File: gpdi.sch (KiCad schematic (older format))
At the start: 20 parts, among them U1 LFE5U-85F-6BG381C, U11 PCA9306D

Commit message: schematics: some PN's for LCSC
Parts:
- GPDI1: LCSC (none) -> C427307
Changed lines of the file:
@@
 F 11 "609-4614-1-ND" H 8950 2950 50  0001 C CNN "Digikey"
 F 12 "A136174CT-ND" H 8950 2950 50  0001 C CNN "Digike_y2"
-F 13 "10029449-111RLF" H 8950 2950 50  0001 C CNN "Onlinecomponents"
-F 14 "0.364$" H 8950 2950 50  0001 C CNN "price100_Onlinecomponents"
-F 15 "FX001" H 8950 2950 50  0001 C CNN "Koncar"
-F 16 "T" H 8950 2950 50  0001 C CNN "Side"
+F 13 "C427307" H 8950 2950 50  0001 C CNN "LCSC"
+F 14 "10029449-111RLF" H 8950 2950 50  0001 C CNN "Onlinecomponents"
+F 15 "0.364$" H 8950 2950 50  0001 C CNN "price100_Onlinecomponents"
+F 16 "FX001" H 8950 2950 50  0001 C CNN "Koncar"
+F 17 "T" H 8950 2950 50  0001 C CNN "Side"
 	1    8950 2950
 	1    0    0    -1

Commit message: LCSC PN's
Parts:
- R24: LCSC (none) -> C73806
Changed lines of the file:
@@
 F 7 "71-CRCW0603100KFKEAC" V 6100 4700 50  0001 C CNN "Mouse_r2"
 F 8 "P100KHCT-ND" V 6100 4700 50  0001 C CNN "Digikey"
-F 9 "FR003" V 6100 4700 50  0001 C CNN "Koncar"
+F 9 "C73806" V 6100 4700 50  0001 C CNN "LCSC"
+F 10 "FR003" V 6100 4700 50  0001 C CNN "Koncar"
 	1    6100 4700
 	1    0    0    -1

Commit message: schematics: switch to serdes symbol
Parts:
- U1: symbol lfe5bg381:LFE5U-85F-6BG381C -> lfe5bg381:LFE5UM-85F-6BG381C
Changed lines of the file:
@@
 	6100 4450 6300 4450
 $Comp
-L lfe5bg381:LFE5U-85F-6BG381C U1
+L lfe5bg381:LFE5UM-85F-6BG381C U1
 U 2 1 5A07A906
 P 3600 2900

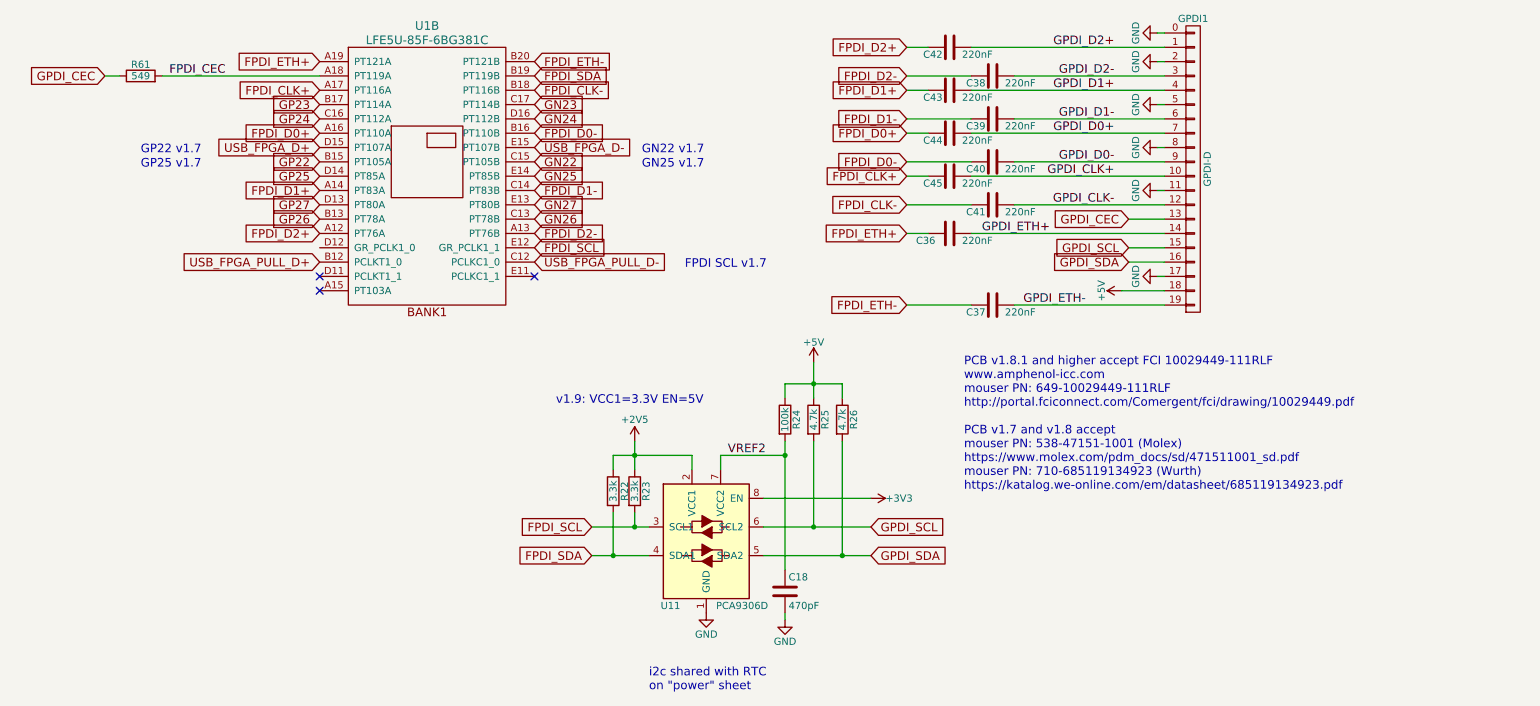
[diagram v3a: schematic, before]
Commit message: schematics: HPD resistor instead of capacitor
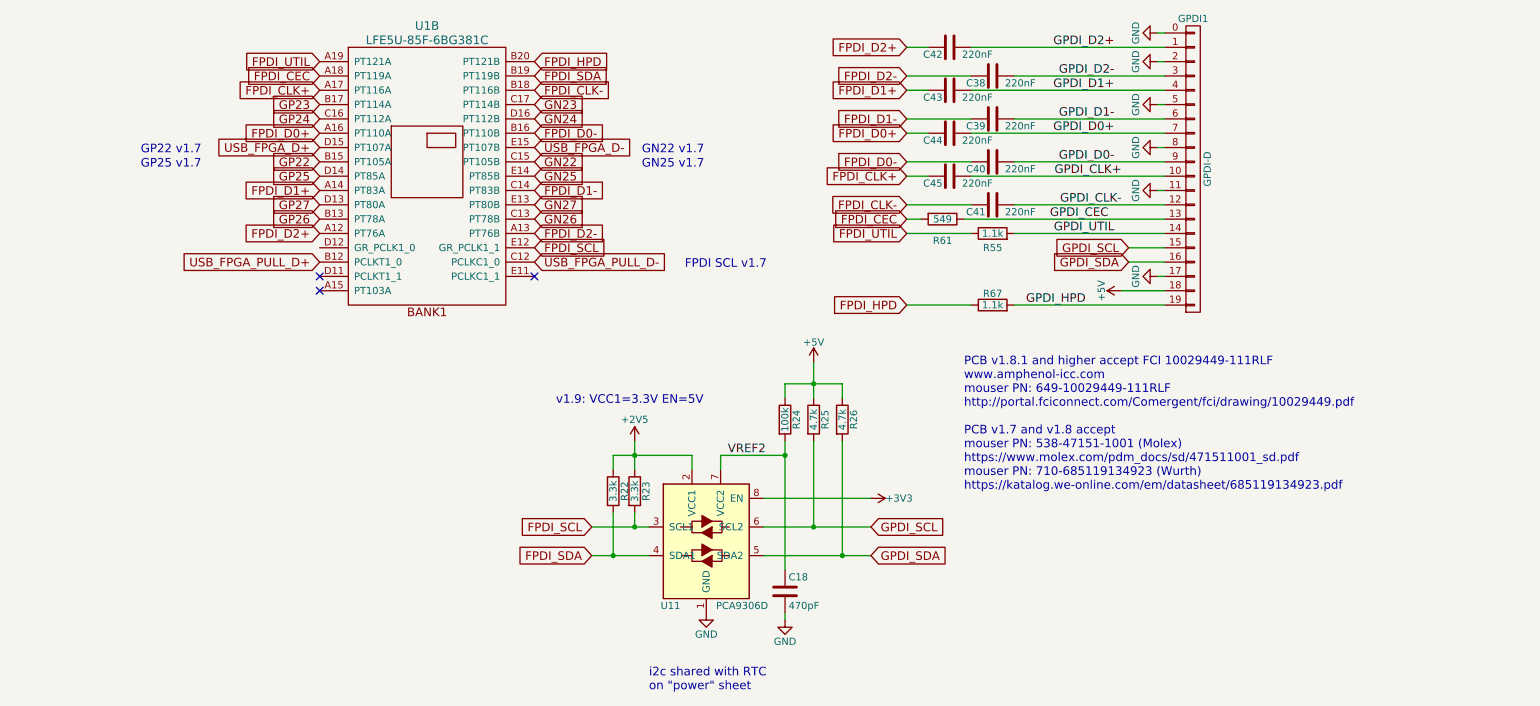
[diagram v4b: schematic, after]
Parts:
- removed C36, C37: 220nF, Capacitor_SMD:C_0603_1608Metric, symbol Device:C
- added R55, R67: 1.1k, Resistor_SMD:R_0603_1608Metric, symbol Device:R
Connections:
- net FPDI_ETH+ renamed FPDI_UTIL
- net FPDI_UTIL: now also R55.1
- net FPDI_ETH- renamed FPDI_HPD
- net FPDI_HPD: now also R67.1
- net GPDI_ETH+ renamed GPDI_UTIL
- net GPDI_UTIL: now also R55.2
- net GPDI_ETH- renamed GPDI_HPD
- net GPDI_HPD: now also R67.2
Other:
- moved on the sheet: R61
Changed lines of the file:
@@
 Title "ULX3S"
 Date ""
-Rev "1.0.2"
+Rev "1.0.3"
 Comp "EMARD"
 Comment1 "General Purpose Differential Interface"
@@
 $EndComp
 Text GLabel 6950 3900 0    60   Input ~ 0
-FPDI_ETH-
+FPDI_HPD
 Text GLabel 6950 3400 0    60   Input ~ 0
-FPDI_ETH+
+FPDI_UTIL
 Text GLabel 6950 2100 0    60   Input ~ 0
 FPDI_D2+
@@
 Text GLabel 6950 3200 0    60   Input ~ 0
 FPDI_CLK-
-Text GLabel 8500 3300 0    60   Input ~ 0
-GPDI_CEC
+Text GLabel 6950 3300 0    60   Input ~ 0
+FPDI_CEC
 Text GLabel 8500 3500 0    60   Input ~ 0
 GPDI_SCL
@@
 FPDI_CLK-
 Text GLabel 4350 2200 2    60   Input ~ 0
-FPDI_ETH-
+FPDI_HPD
 Text GLabel 2850 3100 0    60   Input ~ 0
 FPDI_D1+
@@
 FPDI_CLK+
 Text GLabel 2850 2200 0    60   Input ~ 0
-FPDI_ETH+
+FPDI_UTIL
 Text GLabel 4350 3500 2    60   Input ~ 0
 FPDI_SCL
 Text GLabel 4350 2300 2    60   Input ~ 0
 FPDI_SDA
-Text GLabel 1350 2300 0    60   Input ~ 0
-GPDI_CEC
+Text GLabel 2850 2300 0    60   Input ~ 0
+FPDI_CEC
 Text GLabel 4350 2900 2    60   Input ~ 0
 GN22
@@
 	8750 3200 7700 3200
 Wire Wire Line
-	8750 3300 8500 3300
-Wire Wire Line
-	8750 3400 7400 3400
+	8750 3400 7700 3400
 Wire Wire Line
 	8750 3500 8500 3500
@@
 L Device:R R61
 U 1 1 5A0777ED
-P 1600 2300
-F 0 "R61" V 1680 2300 50  0000 C CNN
-F 1 "549" V 1600 2300 50  0000 C CNN
-F 2 "Resistor_SMD:R_0603_1608Metric" V 1530 2300 50  0001 C CNN
-F 3 "" H 1600 2300 50  0000 C CNN
-	1    1600 2300
-	0    -1   -1   0
-$EndComp
-Wire Wire Line
-	1750 2300 2850 2300
-Wire Wire Line
-	1450 2300 1350 2300
-Text Label 1800 2300 0    60   ~ 0
-FPDI_CEC
+P 7200 3300
+F 0 "R61" V 7350 3300 50  0000 C CNN
+F 1 "549" V 7200 3300 50  0000 C CNN
+F 2 "Resistor_SMD:R_0603_1608Metric" V 7130 3300 50  0001 C CNN
+F 3 "" H 7200 3300 50  0000 C CNN
+	1    7200 3300
+	0    1    1    0
+$EndComp
 Text Notes 5150 6600 0    60   ~ 0
 i2c shared with RTC\non "power" sheet
@@
 USB_FPGA_D-
 $Comp
-L Device:C C36
-U 1 1 5A878883
-P 7250 3400
-F 0 "C36" V 7300 3500 50  0000 L CNN
-F 1 "220nF" V 7300 3100 50  0000 L CNN
-F 2 "Capacitor_SMD:C_0603_1608Metric" H 7288 3250 50  0001 C CNN
-F 3 "" H 7250 3400 50  0000 C CNN
-	1    7250 3400
-	0    -1   1    0
-$EndComp
-$Comp
-L Device:C C37
-U 1 1 5A878B40
-P 7550 3900
-F 0 "C37" V 7600 3950 50  0000 L CNN
-F 1 "220nF" V 7600 3600 50  0000 L CNN
-F 2 "Capacitor_SMD:C_0603_1608Metric" H 7588 3750 50  0001 C CNN
-F 3 "" H 7550 3900 50  0000 C CNN
-	1    7550 3900
-	0    -1   1    0
-$EndComp
-$Comp
 L Device:C C45
 U 1 1 5A87EC41
@@
 	7100 3000 6950 3000
 Wire Wire Line
-	7100 3400 6950 3400
-Text Label 7950 3400 2    60   ~ 0
-GPDI_ETH+
+	7400 3400 6950 3400
+Text Label 8400 3400 2    60   ~ 0
+GPDI_UTIL
 Text Label 8200 3900 2    60   ~ 0
-GPDI_ETH-
-Text Label 8400 3200 2    60   ~ 0
+GPDI_HPD
+Text Label 8450 3200 2    60   ~ 0
 GPDI_CLK-
-Text Label 8400 3000 2    60   ~ 0
+Text Label 8450 3000 2    60   ~ 0
 GPDI_CLK+
 Text Label 8400 2900 2    60   ~ 0
@@
 NoConn ~ 2850 3800
 NoConn ~ 4350 3700
+$Comp
+L Device:R R67
+U 1 1 5F900680
+P 7550 3900
+F 0 "R67" V 7630 3900 50  0000 C CNN
+F 1 "1.1k" V 7550 3900 50  0000 C CNN
+F 2 "Resistor_SMD:R_0603_1608Metric" V 7480 3900 50  0001 C CNN
+F 3 "" H 7550 3900 50  0000 C CNN
+	1    7550 3900
+	0    -1   -1   0
+$EndComp
+$Comp
+L Device:R R55
+U 1 1 5F9109EC
+P 7550 3400
+F 0 "R55" V 7450 3400 50  0000 C CNN
+F 1 "1.1k" V 7550 3400 50  0000 C CNN
+F 2 "Resistor_SMD:R_0603_1608Metric" V 7480 3400 50  0001 C CNN
+F 3 "" H 7550 3400 50  0000 C CNN
+F 4 "Leave empty" V 7550 3400 50  0001 C CNN "Note"
+	1    7550 3400
+	0    -1   -1   0
+$EndComp
+Wire Wire Line
+	7350 3300 8750 3300
+Wire Wire Line
+	7050 3300 6950 3300
+Text Label 7950 3300 0    60   ~ 0
+GPDI_CEC
 $EndSCHEMATC

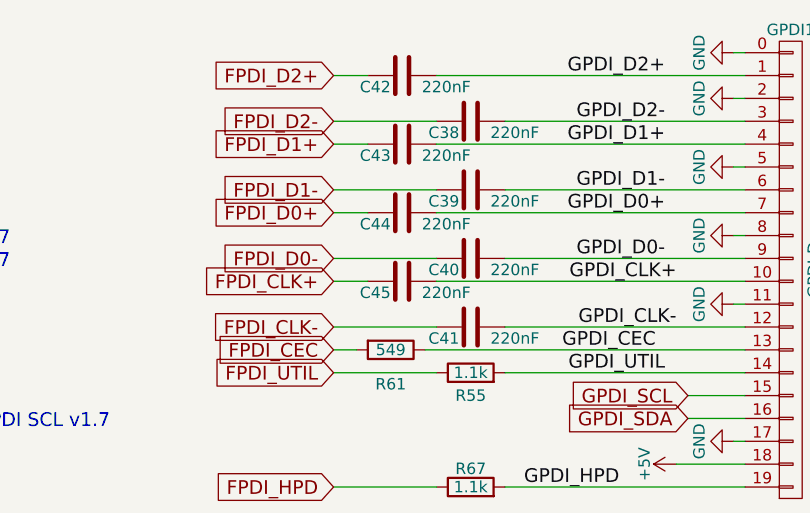
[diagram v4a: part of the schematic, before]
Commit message: schematics: sort GPDI capacitors
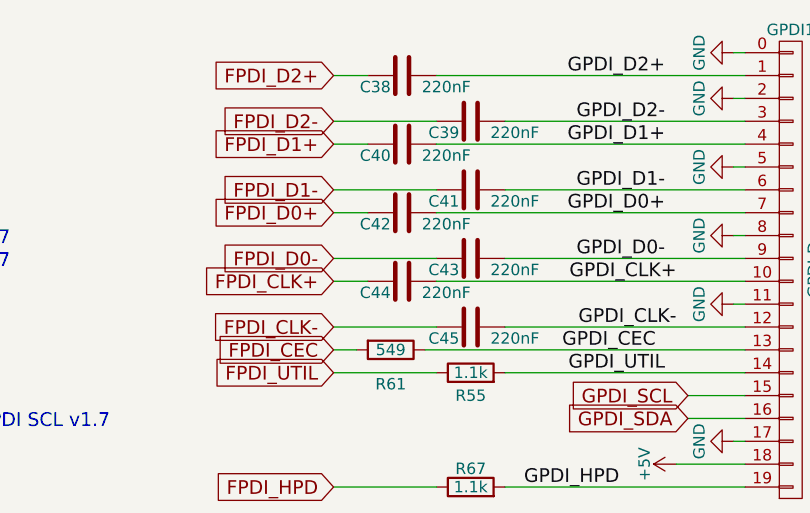
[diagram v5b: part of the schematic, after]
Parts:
- renumbered C42 to C38, C38 to C39, C43 to C40, C39 to C41, C44 to C42, C40 to C43, C45 to C44, C41 to C45
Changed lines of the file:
@@
 USB_FPGA_D-
 $Comp
-L Device:C C45
+L Device:C C44
 U 1 1 5A87EC41
 P 7250 3000
-F 0 "C45" V 7300 3050 50  0000 L CNN
+F 0 "C44" V 7300 3050 50  0000 L CNN
 F 1 "220nF" V 7300 2700 50  0000 L CNN
 F 2 "Capacitor_SMD:C_0603_1608Metric" H 7288 2850 50  0001 C CNN
@@
 $EndComp
 $Comp
-L Device:C C41
+L Device:C C45
 U 1 1 5A87EC93
 P 7550 3200
-F 0 "C41" V 7600 3250 50  0000 L CNN
+F 0 "C45" V 7600 3250 50  0000 L CNN
 F 1 "220nF" V 7600 2900 50  0000 L CNN
 F 2 "Capacitor_SMD:C_0603_1608Metric" H 7588 3050 50  0001 C CNN
@@
 $EndComp
 $Comp
-L Device:C C40
+L Device:C C43
 U 1 1 5A87EEE5
 P 7550 2900
-F 0 "C40" V 7600 2950 50  0000 L CNN
+F 0 "C43" V 7600 2950 50  0000 L CNN
 F 1 "220nF" V 7600 2600 50  0000 L CNN
 F 2 "Capacitor_SMD:C_0603_1608Metric" H 7588 2750 50  0001 C CNN
@@
 $EndComp
 $Comp
-L Device:C C44
+L Device:C C42
 U 1 1 5A87EF45
 P 7250 2700
-F 0 "C44" V 7300 2750 50  0000 L CNN
+F 0 "C42" V 7300 2750 50  0000 L CNN
 F 1 "220nF" V 7300 2400 50  0000 L CNN
 F 2 "Capacitor_SMD:C_0603_1608Metric" H 7288 2550 50  0001 C CNN
@@
 	7400 3200 6950 3200
 $Comp
-L Device:C C39
+L Device:C C41
 U 1 1 5A87F247
 P 7550 2600
-F 0 "C39" V 7600 2650 50  0000 L CNN
+F 0 "C41" V 7600 2650 50  0000 L CNN
 F 1 "220nF" V 7600 2300 50  0000 L CNN
 F 2 "Capacitor_SMD:C_0603_1608Metric" H 7588 2450 50  0001 C CNN
@@
 $EndComp
 $Comp
-L Device:C C43
+L Device:C C40
 U 1 1 5A87F2A7
 P 7250 2400
-F 0 "C43" V 7300 2450 50  0000 L CNN
+F 0 "C40" V 7300 2450 50  0000 L CNN
 F 1 "220nF" V 7300 2100 50  0000 L CNN
 F 2 "Capacitor_SMD:C_0603_1608Metric" H 7288 2250 50  0001 C CNN
@@
 	7400 2600 6950 2600
 $Comp
-L Device:C C42
+L Device:C C38
 U 1 1 5A87F538
 P 7250 2100
-F 0 "C42" V 7300 2150 50  0000 L CNN
+F 0 "C38" V 7300 2150 50  0000 L CNN
 F 1 "220nF" V 7300 1800 50  0000 L CNN
 F 2 "Capacitor_SMD:C_0603_1608Metric" H 7288 1950 50  0001 C CNN
@@
 $EndComp
 $Comp
-L Device:C C38
+L Device:C C39
 U 1 1 5A87F5AA
 P 7550 2300
-F 0 "C38" V 7600 2350 50  0000 L CNN
+F 0 "C39" V 7600 2350 50  0000 L CNN
 F 1 "220nF" V 7600 2000 50  0000 L CNN
 F 2 "Capacitor_SMD:C_0603_1608Metric" H 7588 2150 50  0001 C CNN

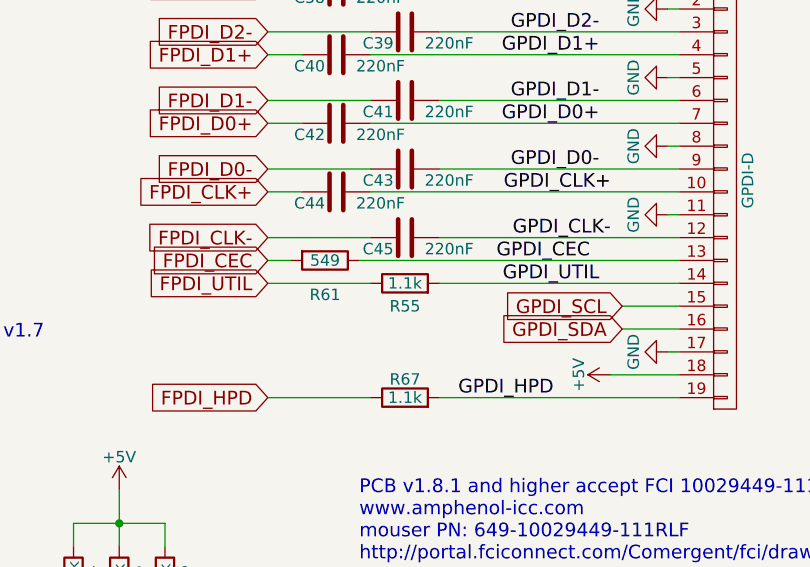
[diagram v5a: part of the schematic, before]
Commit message: schematics: 10k HPD resistor
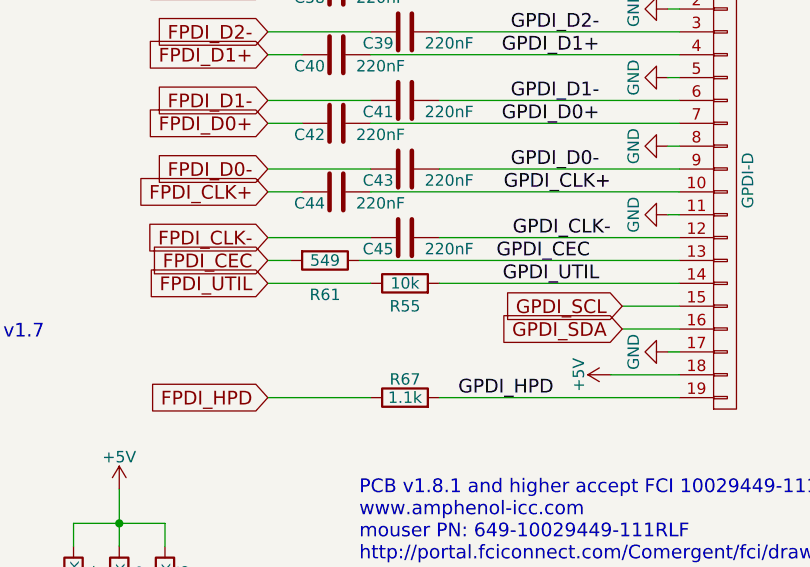
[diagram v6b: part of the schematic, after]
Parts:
- R55: value 1.1k -> 10k
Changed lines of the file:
@@
 P 7550 3400
 F 0 "R55" V 7450 3400 50  0000 C CNN
-F 1 "1.1k" V 7550 3400 50  0000 C CNN
+F 1 "10k" V 7550 3400 50  0000 C CNN
 F 2 "Resistor_SMD:R_0603_1608Metric" V 7480 3400 50  0001 C CNN
 F 3 "" H 7550 3400 50  0000 C CNN

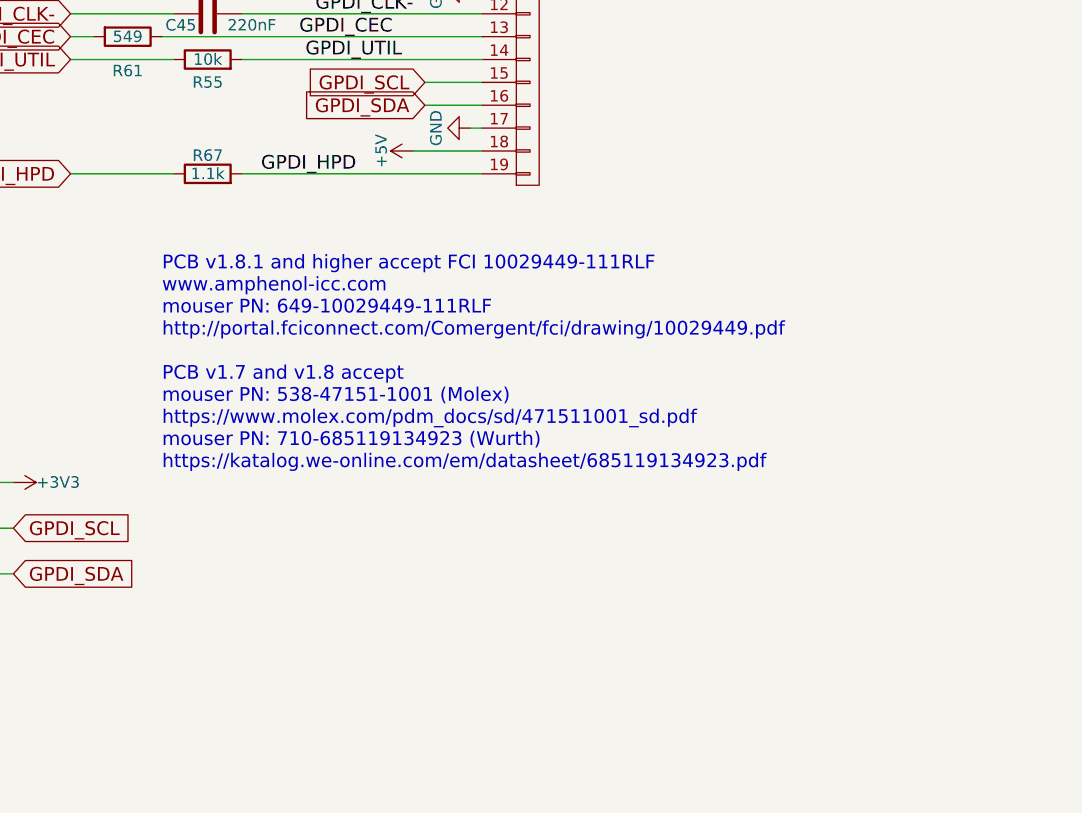
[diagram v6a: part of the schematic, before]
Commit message: schematics: D30 zener 3.6V for HPD protection and 549 ohm resistor
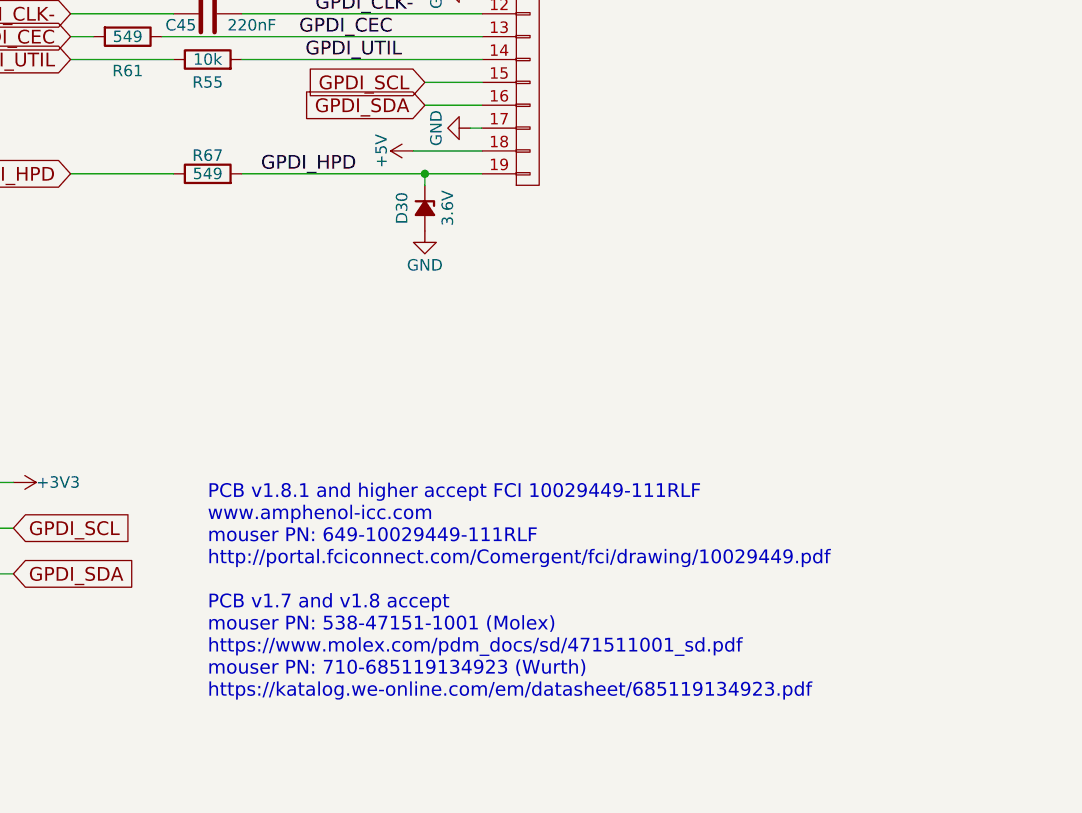
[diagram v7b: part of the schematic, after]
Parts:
- added D30: 3.6V, Diode_SMD:D_SOD-323_HandSoldering, symbol Device:D_Zener_Small_ALT
- R67: value 1.1k -> 549
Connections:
- net GND: now also D30.2 (A)
- net GPDI_HPD: now also D30.1 (K)
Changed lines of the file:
@@
 	8750 3700 8700 3700
 Wire Wire Line
-	8750 3900 7700 3900
+	8750 3900 8500 3900
 Wire Wire Line
 	8750 3800 8450 3800
@@
 Wire Wire Line
 	5050 5450 5150 5450
-Text Notes 7350 5200 0    60   ~ 0
+Text Notes 7550 6200 0    60   ~ 0
 PCB v1.8.1 and higher accept FCI 10029449-111RLF\nwww.amphenol-icc.com\nmouser PN: 649-10029449-111RLF\nhttp://portal.fciconnect.com/Comergent/fci/drawing/10029449.pdf\n\nPCB v1.7 and v1.8 accept\nmouser PN: 538-47151-1001 (Molex)\nhttps://www.molex.com/pdm_docs/sd/471511001_sd.pdf\nmouser PN: 710-685119134923 (Wurth)\nhttps://katalog.we-online.com/em/datasheet/685119134923.pdf
 $Comp
@@
 P 7550 3900
 F 0 "R67" V 7630 3900 50  0000 C CNN
-F 1 "1.1k" V 7550 3900 50  0000 C CNN
+F 1 "549" V 7550 3900 50  0000 C CNN
 F 2 "Resistor_SMD:R_0603_1608Metric" V 7480 3900 50  0001 C CNN
 F 3 "" H 7550 3900 50  0000 C CNN
 	1    7550 3900
 	0    -1   -1   0
+$EndComp
+Wire Wire Line
+	7350 3300 8750 3300
+Wire Wire Line
+	7050 3300 6950 3300
+Text Label 7950 3300 0    60   ~ 0
+GPDI_CEC
+$Comp
+L Device:D_Zener_Small_ALT D?
+U 1 1 5F8E4470
+P 8500 4050
+AR Path="/58D6BF46/5F8E4470" Ref="D?"  Part="1"
+AR Path="/58D686D9/5F8E4470" Ref="D30"  Part="1"
+F 0 "D30" H 8500 3950 50  0000 C CNN
+F 1 "3.6V" H 8500 4150 50  0000 C CNN
+F 2 "Diode_SMD:D_SOD-323_HandSoldering" V 8500 4050 50  0001 C CNN
+F 3 "http://www.taiwansemi.com/products/datasheet/BZT52C2V4S%20SERIES_H1709.pdf" V 8500 4050 50  0001 C CNN
+	1    8500 4050
+	0    1    1    0
+$EndComp
+Wire Wire Line
+	8500 3900 8500 3950
+Connection ~ 8500 3900
+Wire Wire Line
+	8500 3900 7700 3900
+$Comp
+L power:GND #PWR043
+U 1 1 5F8F4E63
+P 8500 4150
+F 0 "#PWR043" H 8500 3900 50  0001 C CNN
+F 1 "GND" H 8500 4000 50  0000 C CNN
+F 2 "" H 8500 4150 50  0000 C CNN
+F 3 "" H 8500 4150 50  0000 C CNN
+	1    8500 4150
+	1    0    0    -1
 $EndComp
 $Comp
@@
 	0    -1   -1   0
 $EndComp
-Wire Wire Line
-	7350 3300 8750 3300
-Wire Wire Line
-	7050 3300 6950 3300
-Text Label 7950 3300 0    60   ~ 0
-GPDI_CEC
 $EndSCHEMATC
